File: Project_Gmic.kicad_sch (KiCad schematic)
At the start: 51 parts, among them J1 USB4085-GF-A, J2 SJ1-3523N, SW1 PCM12SMTR, U1 MCP6479, U2 AD8531, U3 AD8531, U4 MAX1852

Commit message: finishing the simulation, began schematic
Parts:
- removed unit 1 of U1
- removed unit 4 of U1
- removed U2: AD8531, Package_TO_SOT_SMD:SOT-23-5, symbol Custom:AD8531
- added C22: 2.2uF, symbol Device:C
- added R16, R17: 10k, Resistor_SMD:R_0805_2012Metric, symbol Device:R
- added R20, R21: 100k, Resistor_SMD:R_0805_2012Metric, symbol Device:R
- added U2, U7, U8: AD8532, symbol Custom:AD8532
- added U5: AD8531, Package_TO_SOT_SMD:SOT-23-5, symbol Custom:AD8531
- R6, R7: value 2.2k -> 100k
- R9: value 100k -> 50k
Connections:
- net AUDIO_1_IN: now also R20.2, U7.2 (-); no longer R6.2
- net AUDIO_2_IN: now also R21.2, U7.6 (-); no longer R7.2
- net AUDIO_AVERAGE: now also U8.1
- net AUDIO_OUT: no longer RV1.1
- net AUDIO_PASS_LOW: no longer C6.1
- net GNDA: now also C22.2, R17.2, U2.4 (V-), U5.2 (V-), U7.4 (V-), U8.4 (V-)
- net at R6.1, R7.1: now also RV1.2, U8.2 (-); no longer R9.2
- net at R10.1, R12.2: now also C6.1; no longer C6.2
- net at R10.2: now also U8.6 (-), U8.7
- net at C4.2, R5.1: now also U8.5 (+)
- net at C9.2, R12.1: now also U2.3 (+)
- new net: R20.1, R6.2, U7.1
- new net: R21.1, R7.2, U7.7
- new net: R9.2, RV1.3
- new net: C22.1, R16.2, R17.1, U5.3 (+)
- new net: C6.2, U2.1, U2.2 (-)
- new net +3.3V: R16.1, U2.8 (V+), U5.5 (V+), U7.8 (V+), U8.8 (V+)
- new net V_OFFSET: U5.1, U5.4 (-), U7.3 (+), U7.5 (+), U8.3 (+)
- now unconnected: R15.1
- no-connect marks 9 -> 10
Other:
- note added: "Offset reference of Vcc/2"
- moved on the sheet: C4, R5, R6, R7, R9

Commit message: updating schematic, updating BOM
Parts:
- removed C10, C12, C15, C16: 1uF, Capacitor_SMD:C_0805_2012Metric, symbol Device:C_Polarized
- removed C13, C3: 100nF, Capacitor_SMD:C_0805_2012Metric, symbol Device:C
- removed L1, L2: BLM21PG331SN1D, Inductor_SMD:L_0805_2012Metric, symbol Device:L_Ferrite
- removed R14: 100k, Resistor_SMD:R_0805_2012Metric, symbol Device:R
- removed R15, R8: 80k, Resistor_SMD:R_0805_2012Metric, symbol Device:R
- removed U1: MCP6479, Package_SO:SOIC-14_3.9x8.7mm_P1.27mm, symbol Custom:MCP6479
- removed unit 2 of U2
- removed U3: AD8531, Package_TO_SOT_SMD:SOT-23-5, symbol Custom:AD8531
- removed U4: MAX1852, Package_TO_SOT_SMD:SOT-363_SC-70-6_Handsoldering, symbol Custom:MAX1852
- added C10, C16, C24: 100nF, Capacitor_SMD:C_0805_2012Metric, symbol Device:C
- added C12: 2.2uF, Capacitor_SMD:C_0805_2012Metric, symbol Device:C
- added C15, C22, C23, C9: 1uF, Capacitor_SMD:C_0805_2012Metric, symbol Device:C
- added unit 2 of U3
- added U5: TC1055, Package_TO_SOT_SMD:SOT-23-5, symbol Regulator_Linear:TC1055
- C11, C17, C19: value 100nF -> 1uF
- C13: renamed from C22; footprint (none) -> Capacitor_SMD:C_0805_2012Metric
- C20: value 100nF -> 2.2uF
- C21: value NC -> 100nF
- RV1: value PTV09A-5025F-A503 -> PTV09A-4020F-A504; footprint Potentiometer_THT:Potentiometer_Alpha_RD901F-40-00D_Single_Vertical_CircularHoles -> PTV09A-4:PTV09A-4
- U1: renamed from U7; footprint (none) -> Package_SO:SOIC-8_3.9x4.9mm_P1.27mm
- U2: renamed from U8; footprint (none) -> Package_SO:SOIC-8_3.9x4.9mm_P1.27mm
- U3: renamed from U2; footprint (none) -> Package_SO:SOIC-8_3.9x4.9mm_P1.27mm
- renumbered C5 to C3, C8 to C5, C9 to C8, R6 to R10, R7 to R11, R10 to R12, R12 to R13, R9 to R14, R16 to R15, R17 to R16, R3 to R2, R2 to R3, R11 to R6, R13 to R7, R20 to R8, R21 to R9, U5 to U4
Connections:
- net -5V is gone; now on net GNDA: C11.2, C18.2, C19.2, C20.2
- net GND is gone; now on net GNDA: J1.A1 (GND), J1.A12 (GND), J1.B1 (GND), J1.B12 (GND), J1.S1 (SHIELD), R2.2, R4.2
- net +3.3V: now also C11.1, C14.1, C17.1, C7.1, R1.1, R3.1, C10.1, C15.1, C16.1, C23.1, C24.1, C9.1, U5.5 (Vout)
- net +5V: now also C18.1, C19.1, C20.1, C21.1, C22.1, U5.1 (Vin), U5.3 (~{SHDN}); no longer C14.1, C17.1, C7.1, R1.1, R3.1
- net AUDIO_OUT: now also C12.1
- net AUDIO_PASS_HIGH: now also C12.2, U3.6 (-), U3.7
- net AUDIO_PASS_LOW: now also C3.2, C6.1, U3.1, U3.2 (-)
- net GNDA: now also C21.2, C10.2, C15.2, C16.2, C22.2, C23.2, C24.2, C9.2, U5.2 (GND); no longer C11.1, C18.1, C19.1, C20.1, R7.1
- net V_OFFSET: now also R7.1
- net at C5.1, R7.2: now also U3.5 (+)
- net at SW1.2 (B): now also J2.2, J2.3; no longer C21.2
- net at R12.1, R13.2: now also C6.2; no longer C6.1
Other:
- note added: "CC removing, audio output"
- note added: "Decoupling"
- note added: "High-pass filter 20Hz, 2 order"
- note added: "Low-pass filter 20kHz, 3 order"
- note added: "Pre-amp (current to voltage) and audio average"
- note removed: "Audio average and pre-amp"
- note removed: "Bypass"
- note removed: "High-pass Filter"
- note removed: "Last amplification"
- note removed: "Low-pass Filter"
- moved on the sheet: C13, C3, C4, C5, C6, C8, H1, H2, H3, R10, R11, R12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

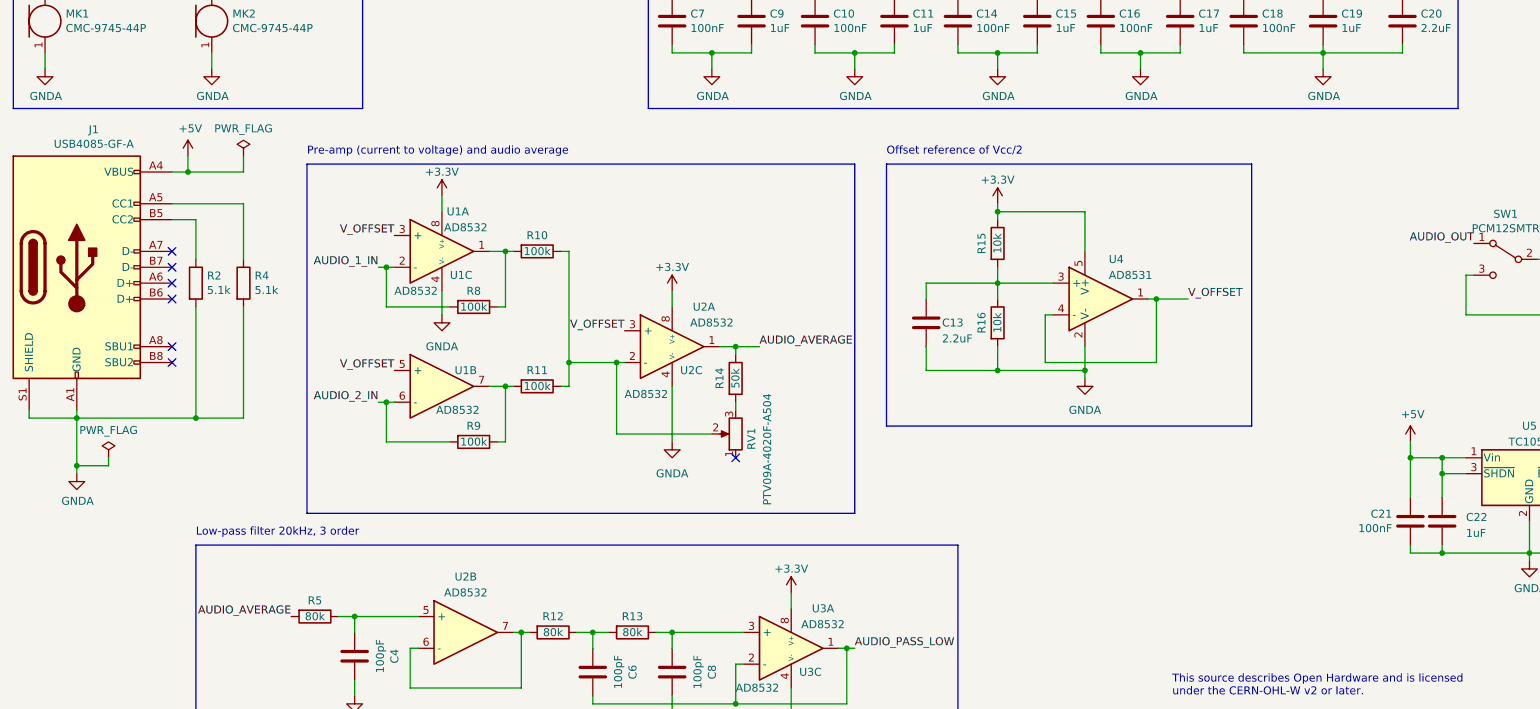
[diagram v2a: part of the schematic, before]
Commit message: fixing pcb error, reset footprints from libs, add diode
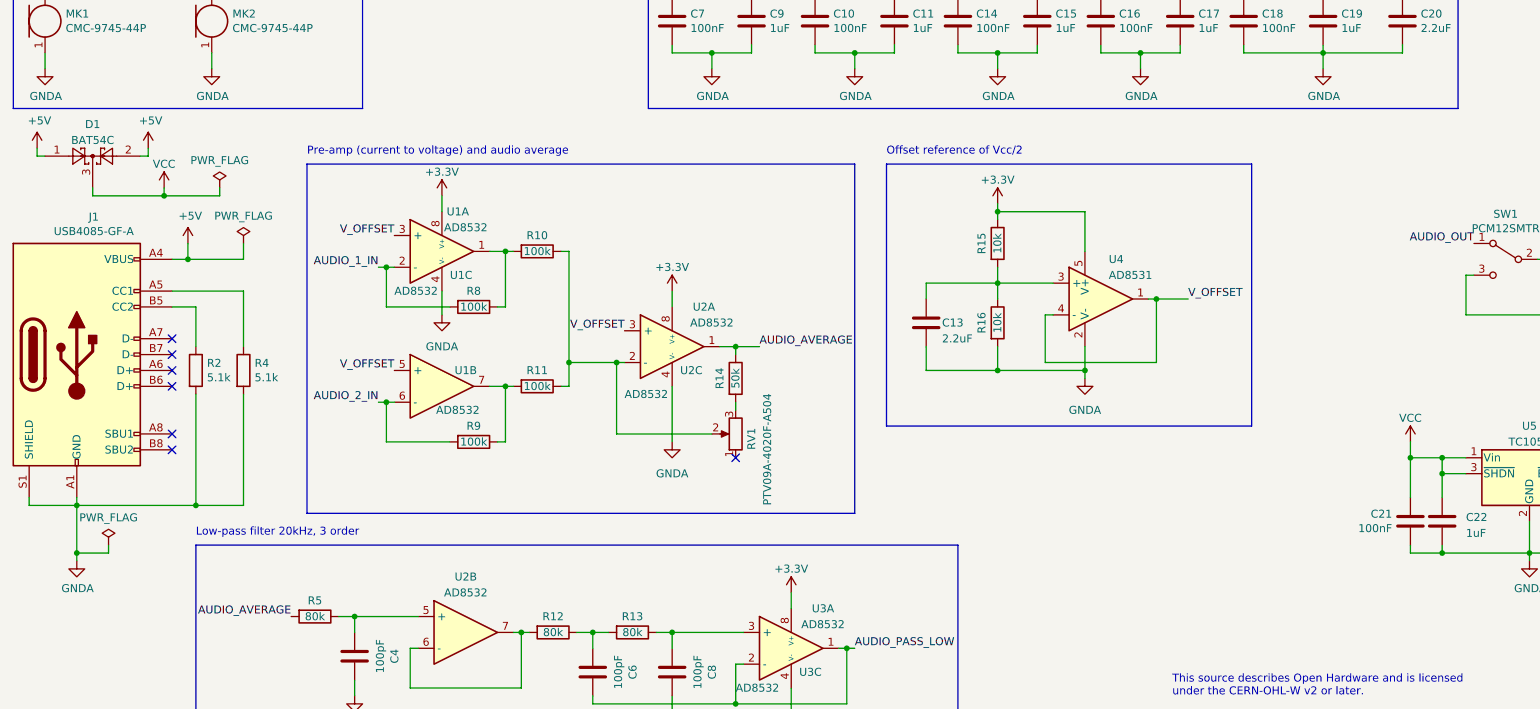
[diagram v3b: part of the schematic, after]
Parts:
- added D1: BAT54C, Package_TO_SOT_SMD:SOT-23, symbol Diode:BAT54C
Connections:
- net +5V: now also D1.1, D1.2; no longer C21.1, C22.1, U5.1 (Vin), U5.3 (~{SHDN})
- new net VCC: C21.1, C22.1, D1.3, U5.1 (Vin), U5.3 (~{SHDN})
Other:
- moved on the sheet: J1, R2, R4

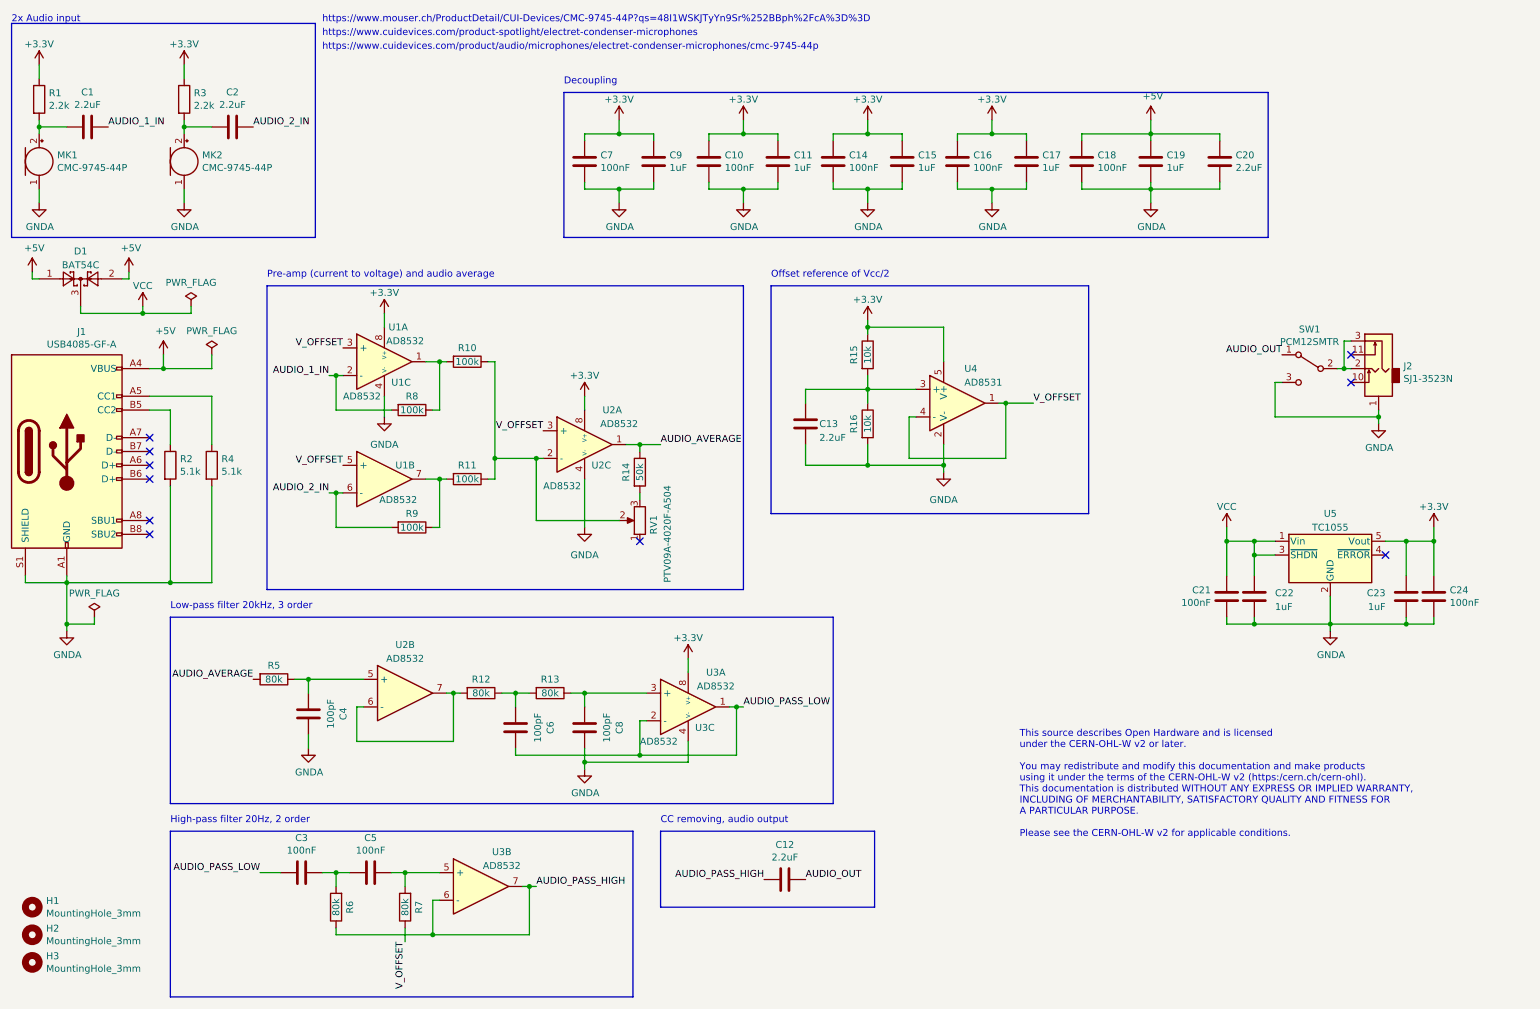
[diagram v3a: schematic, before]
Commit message: working on a v1.2, better USB isolation, audio output isolation
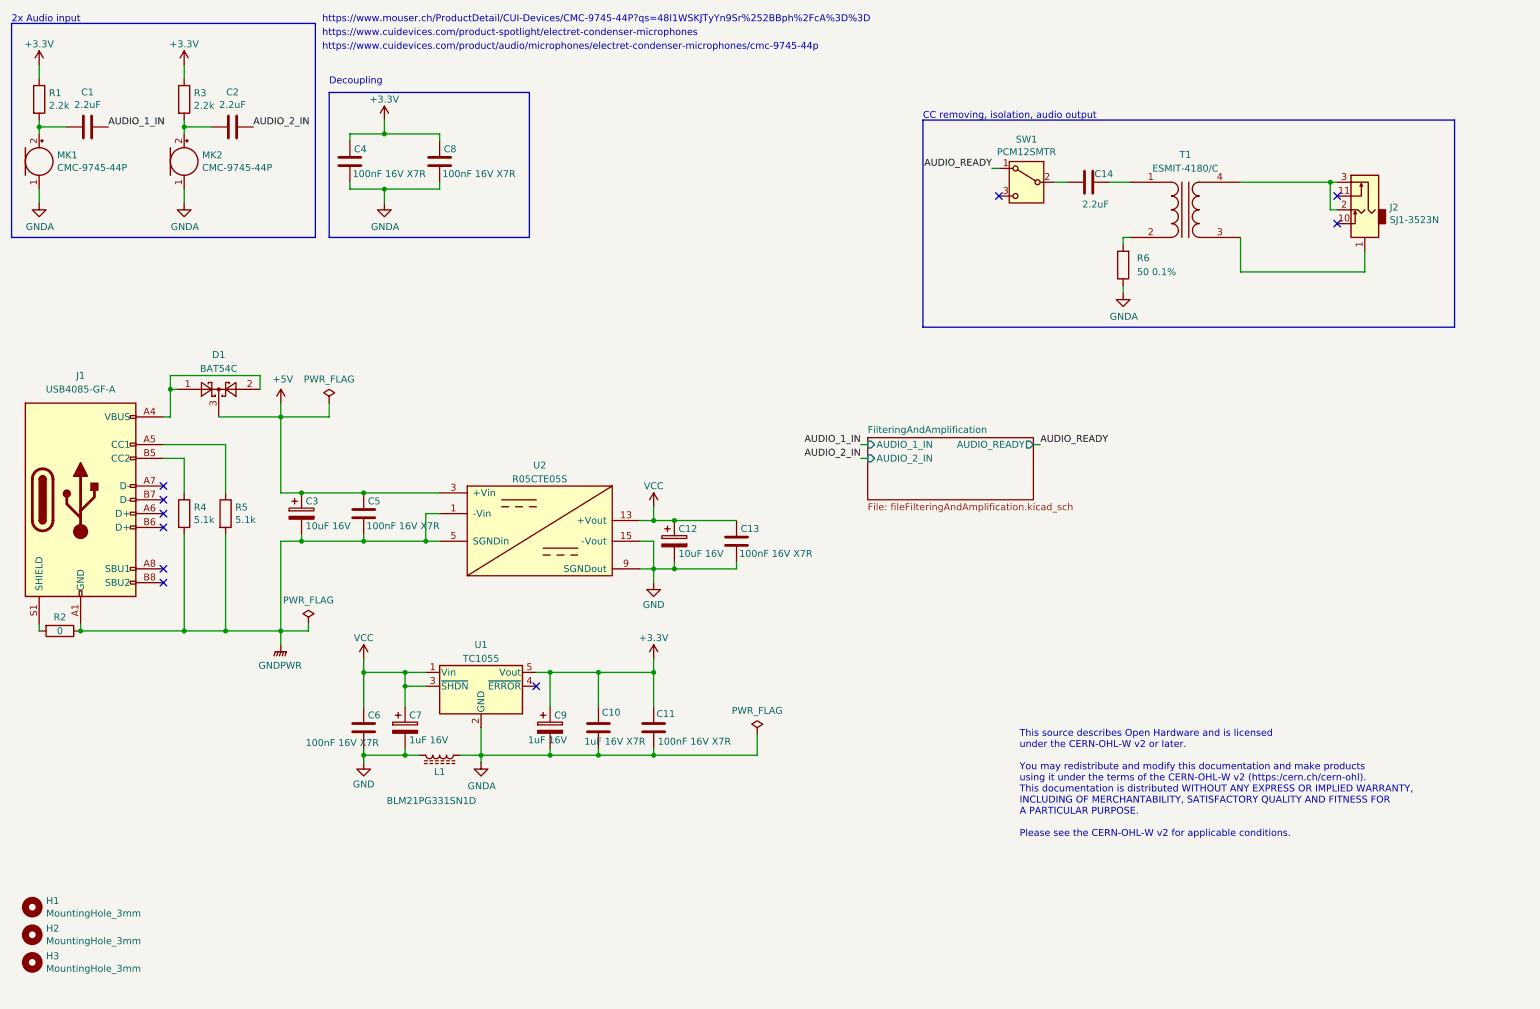
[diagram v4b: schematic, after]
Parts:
- removed C10, C16, C18, C21, C3, C7: 100nF, Capacitor_SMD:C_0805_2012Metric, symbol Device:C
- removed C11, C15, C17, C19, C22, C9: 1uF, Capacitor_SMD:C_0805_2012Metric, symbol Device:C
- removed C12, C20: 2.2uF, Capacitor_SMD:C_0805_2012Metric, symbol Device:C
- removed J1: USB4085-GF-A, Connector_USB:USB_C_Receptacle_GCT_USB4085, symbol Connector:USB_C_Receptacle_USB2.0
- removed R10, R11, R8, R9: 100k, Resistor_SMD:R_0805_2012Metric, symbol Device:R
- removed R12, R13, R5, R7: 80k, Resistor_SMD:R_0805_2012Metric, symbol Device:R
- removed R14: 50k, Resistor_SMD:R_0805_2012Metric, symbol Device:R
- removed R15, R16: 10k, Resistor_SMD:R_0805_2012Metric, symbol Device:R
- removed RV1: PTV09A-4020F-A504, PTV09A-4:PTV09A-4, symbol Device:R_Potentiometer
- removed U1, U2, U3: AD8532, Package_SO:SOIC-8_3.9x4.9mm_P1.27mm, symbol Custom:AD8532
- removed U4: AD8531, Package_TO_SOT_SMD:SOT-23-5, symbol Custom:AD8531
- added C12, C3: 10uF 16V, symbol Device:C_Polarized
- added C7, C9: 1uF 16V, symbol Device:C_Polarized
- added J1: USB4085-GF-A, symbol Connector:USB_C_Receptacle_USB2.0_16P
- added L1: BLM21PG331SN1D, symbol Device:L_Ferrite
- added R2: 0, symbol Device:R
- added T1: ESMIT-4180/C, symbol Device:Transformer_1P_1S
- added U2: R05CTE05S, Package_SO:SOIC-16W_7.5x10.3mm_P1.27mm, symbol Custom:R05CTE05S
- C10: renamed from C23; value 1uF -> 1uF 16V X7R
- C11: renamed from C24; value 100nF -> 100nF 16V X7R
- C13: value 2.2uF -> 100nF 16V X7R; footprint Capacitor_SMD:C_0805_2012Metric -> (none)
- C14: value 100nF -> 2.2uF
- C4, C6, C8: value 100pF -> 100nF 16V X7R; footprint Capacitor_SMD:C_0805_2012Metric -> (none)
- C5: value 100nF -> 100nF 16V X7R; footprint Capacitor_SMD:C_0805_2012Metric -> (none)
- R6: value 80k -> 50 0.1%; footprint Resistor_SMD:R_0805_2012Metric -> (none)
- renumbered R2 to R4, R4 to R5, U5 to U1
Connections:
- net AUDIO_PASS_HIGH is gone; now on net GNDA: R6.1
- net AUDIO_PASS_LOW is gone; now on net VCC: C6.1
- net +3.3V: now also C4.1, C8.1, C9.1; no longer C14.1
- net +5V: now also C5.1, D1.3, C3.1, U2.3 (+Vin), U2.4 (+Vin); no longer D1.1, D1.2
- net GNDA: now also C4.2, C8.2, C9.2, L1.1; no longer C13.2, C14.2, C4.1, C8.1, J2.1, R4.2, R5.2, SW1.3 (C)
- net VCC: now also C13.1, C12.1, C7.1, U2.13 (+Vout), U2.14 (+Vout); no longer D1.3
- net at R6.2: now also T1.2 (AB); no longer C5.2
- net at R4.1: now also J1.B5 (CC2)
- net at R5.1: now also J1.A5 (CC1)
- net at J2.2, J2.3: now also T1.4 (SB); no longer SW1.2 (B)
- net GND: now reaches C6.2
- net GND: now also C13.2, C12.2, C7.2, L1.2, U2.11 (SGNDout), U2.12 (SGNDout), U2.15 (-Vout), U2.16 (-Vout), U2.9 (SGNDout)
- net AUDIO_OUT renamed AUDIO_READY
- new net: J2.1, T1.3 (SA)
- new net: D1.1, D1.2, J1.A4 (VBUS), J1.A9 (VBUS), J1.B4 (VBUS), J1.B9 (VBUS)
- new net: J1.S1 (SHIELD), R2.2
- new net: C14.1, T1.1 (AA)
- new net: C14.2, SW1.2 (B)
- new net -Vin: C3.2, C5.2, J1.A1 (GND), J1.A12 (GND), J1.B1 (GND), J1.B12 (GND), R2.1, R4.2, R5.2, U2.1 (-Vin), U2.2 (-Vin), U2.5 (SGNDin), U2.6 (SGNDin), U2.7 (SGNDin), U2.8 (SGNDin)
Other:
- added sheet FilteringAndAmplification (fileFilteringAndAmplification.kicad_sch)
- note added: "CC removing, isolation, audio output"
- note removed: "CC removing, audio output"
- note removed: "High-pass filter 20Hz, 2 order"
- note removed: "Low-pass filter 20kHz, 3 order"
- note removed: "Offset reference of Vcc/2"
- note removed: "Pre-amp (current to voltage) and audio average"
- moved on the sheet: C10, C11, D1, J2, R4, R5, U1
